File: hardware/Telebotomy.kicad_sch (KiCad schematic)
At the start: 21 parts, among them J2 RJHSE-5080, U1 KSZ8863MLL, U2 ATTINY85-20PU

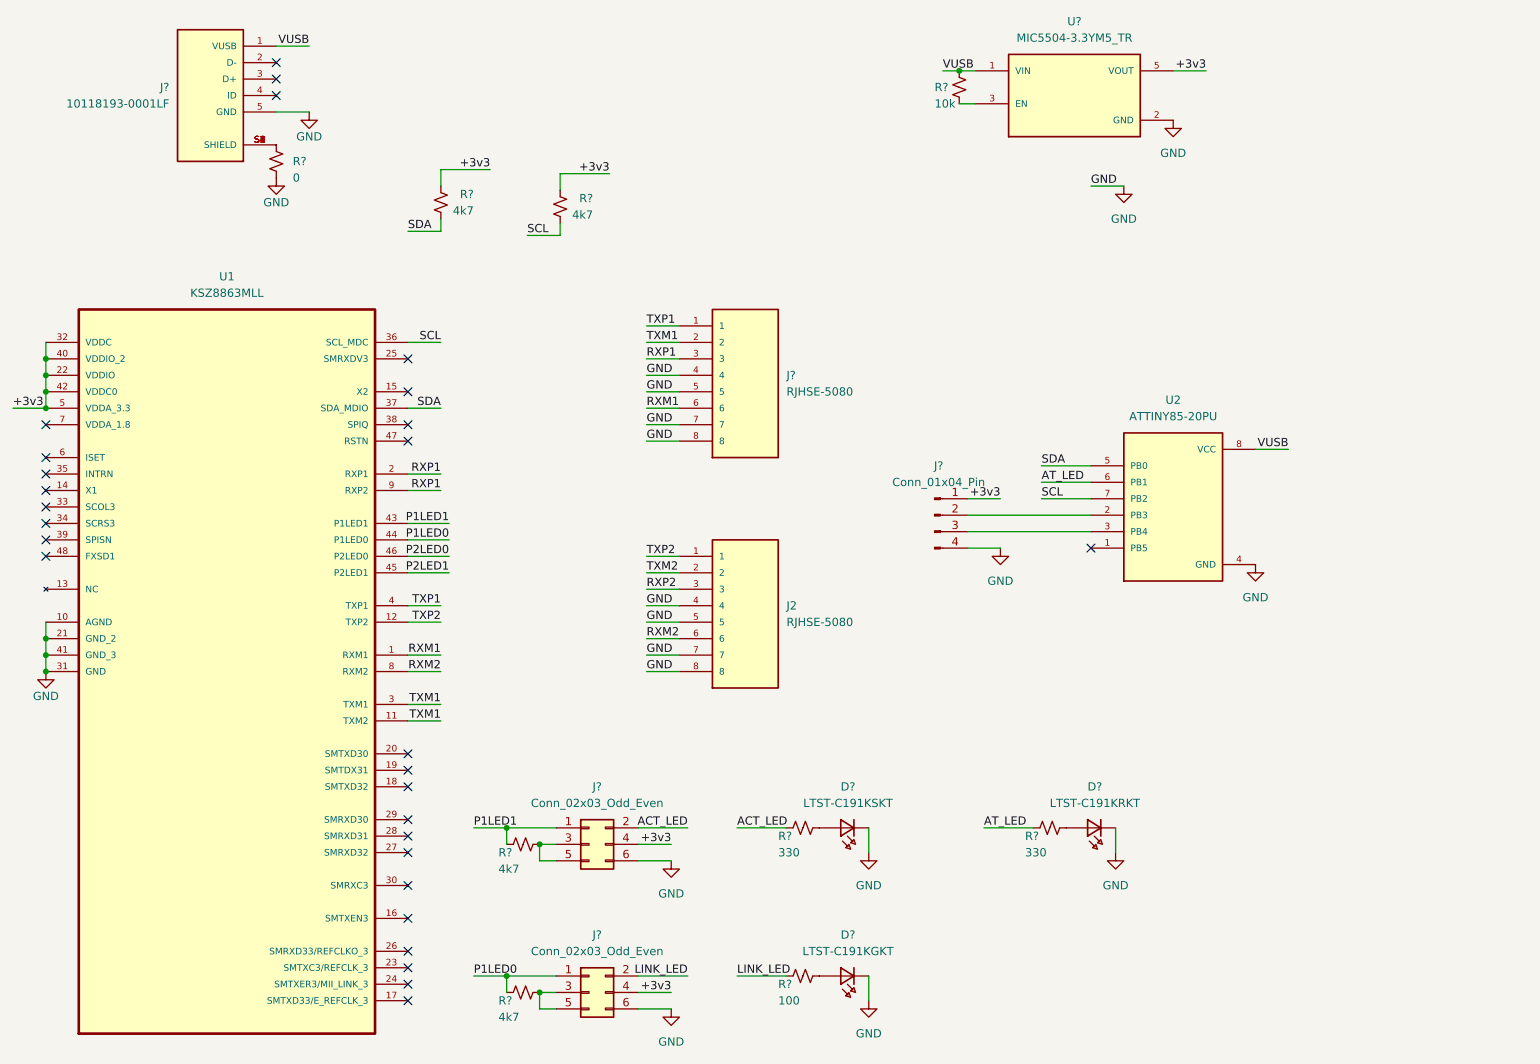
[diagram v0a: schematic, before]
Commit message: Refined schematic and began PCB organization
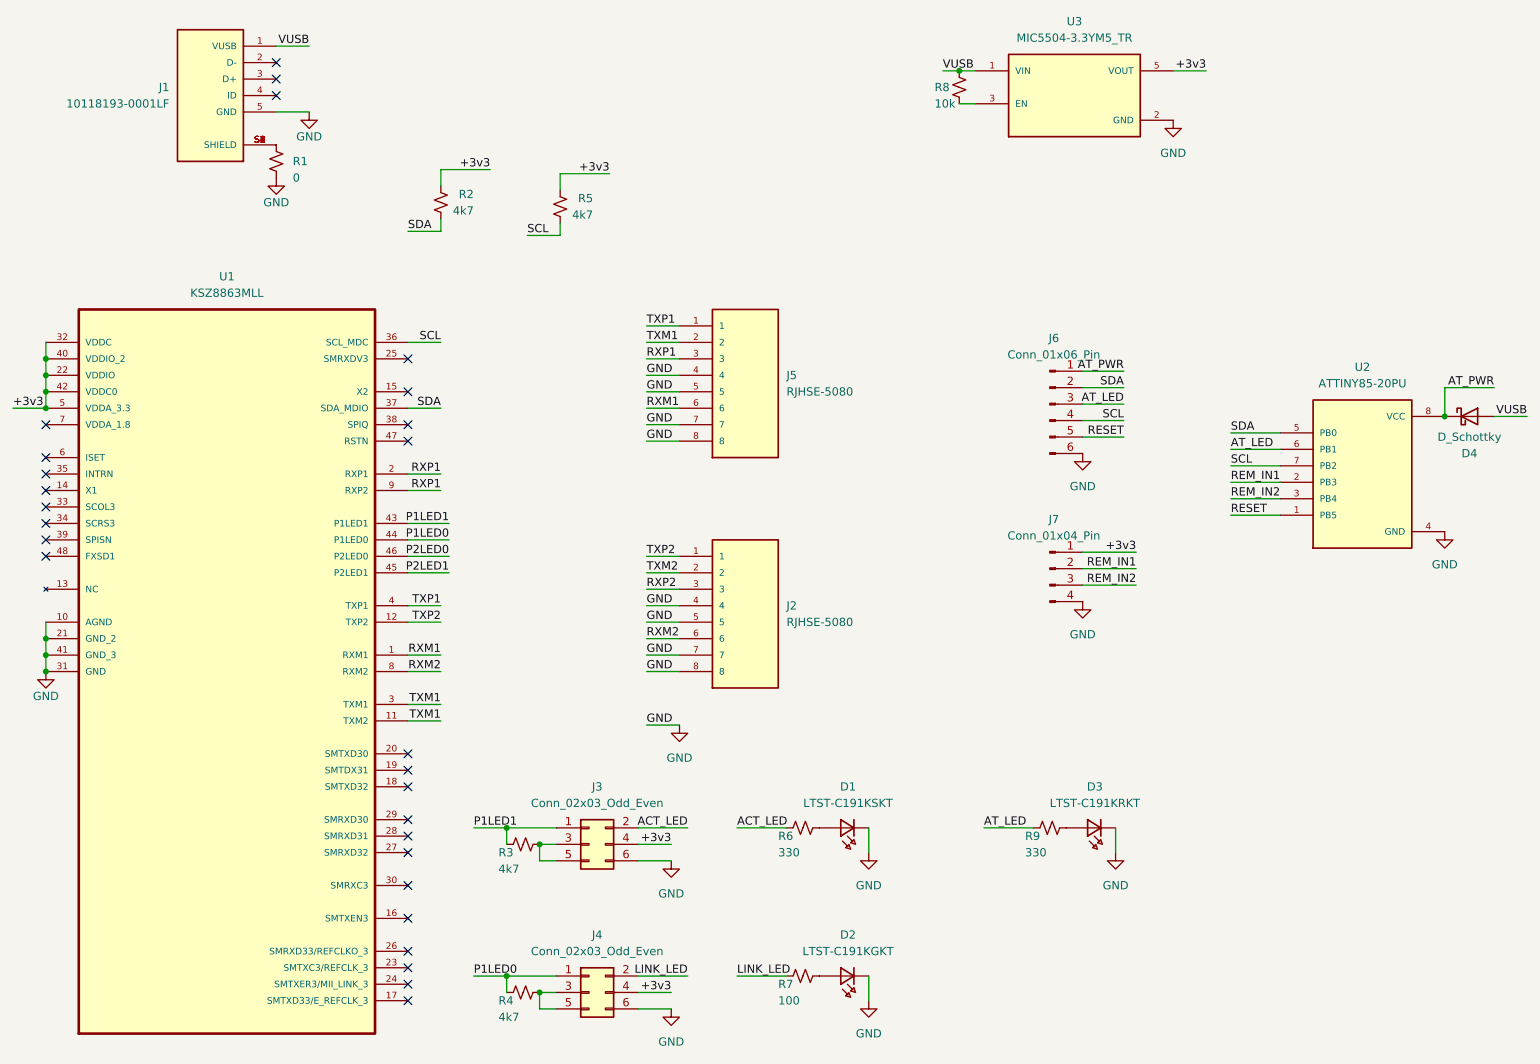
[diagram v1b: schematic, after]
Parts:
- removed J?: Conn_01x04_Pin, symbol Connector:Conn_01x04_Pin
- added D4: D_Schottky, telebotomy:3v3_TVS, symbol Device:D_Schottky
- added J6: Conn_01x06_Pin, Connector_PinHeader_2.54mm:PinHeader_1x06_P2.54mm_Vertical, symbol Connector:Conn_01x06_Pin
- added J7: Conn_01x04_Pin, Connector_PinHeader_2.54mm:PinHeader_1x04_P2.54mm_Vertical, symbol Connector:Conn_01x04_Pin
- D1, D2, D3: renamed from D?; footprint 0603 -> Resistor_SMD:R_0603_1608Metric_Pad0.98x0.95mm_HandSolder
- J1: renamed from J?; footprint AMPHENOL_10118193-0001LF -> telebotomy:AMPHENOL_10118193-0001LF
- J2: footprint AMPHENOL_RJHSE-5080 -> telebotomy:AMPHENOL_RJHSE-5080
- J3, J4: renamed from J?; footprint (none) -> Connector_PinHeader_2.54mm:PinHeader_2x03_P2.54mm_Vertical
- J5: renamed from J?; footprint AMPHENOL_RJHSE-5080 -> telebotomy:AMPHENOL_RJHSE-5080
- R1, R2, R3, R4, R5, R6, R7, R8, R9: renamed from R?; footprint (none) -> Resistor_SMD:R_0603_1608Metric_Pad0.98x0.95mm_HandSolder
- U1: footprint QFP50P900X900X160-48N -> telebotomy:QFP50P900X900X160-48N
- U2: footprint DIP762W46P254L927H533Q8B -> telebotomy:DIP762W46P254L927H533Q8B
- U3: renamed from U?; footprint SOT95P280X145-5N -> telebotomy:SOT95P280X145-5N
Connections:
- net +3v3: now also J7.1 (Pin_1)
- net AT_LED: now also J6.3 (Pin_3)
- net GND: now also J6.6 (Pin_6), J7.4 (Pin_4)
- net SCL: now also J6.4 (Pin_4)
- net SDA: now also J6.2 (Pin_2)
- net VUSB: now also D4.2 (A); no longer U2.8 (VCC)
- net RESET: now reaches U2.1 (PB5)
- net RESET: now also J6.5 (Pin_5)
- net REM_IN1: now reaches U2.2 (PB3)
- net REM_IN1: now also J7.2 (Pin_2)
- net REM_IN2: now reaches U2.3 (PB4)
- net REM_IN2: now also J7.3 (Pin_3)
- new net AT_PWR: D4.1 (K), J6.1 (Pin_1), U2.8 (VCC)
- no-connect marks 28 -> 27
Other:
- moved on the sheet: U2

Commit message: PCB Updates
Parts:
- added TP1, TP2: TestPoint, TestPoint:TestPoint_Pad_D1.0mm, symbol Connector:TestPoint
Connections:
- net REM_IN1: now also U2.3 (PB4), TP1.1; no longer U2.2 (PB3)
- net REM_IN2: now also U2.2 (PB3), TP2.1; no longer U2.3 (PB4)
- net RXM1 renamed RX1_N
- net RX1_N: now also J2.6; no longer J5.6
- net RXM2 renamed RX2_N
- net RX2_N: now also J5.6; no longer J2.6
- net RXP1 renamed RX2_P
- net RX2_P: no longer U1.2 (RXP1)
- net RXP2 renamed RX1_P
- net RX1_P: now also U1.2 (RXP1)
- net TXM1 renamed TX2_N
- net TX2_N: no longer U1.3 (TXM1)
- net TXM2 renamed TX1_N
- net TX1_N: now also U1.3 (TXM1)
- net TXP1 renamed TX1_P
- net TX1_P: now also J2.1; no longer J5.1
- net TXP2 renamed TX2_P
- net TX2_P: now also J5.1; no longer J2.1
